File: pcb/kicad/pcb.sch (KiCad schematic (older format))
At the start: 98 parts, among them K00 KEYSW, K01 KEYSW, K02 KEYSW, K03 KEYSW, K04 KEYSW, K05 KEYSW, K10 KEYSW, K11 KEYSW, K12 KEYSW, K13 KEYSW, K14 KEYSW, K15 KEYSW, K20 KEYSW, K21 KEYSW, K22 KEYSW, K23 KEYSW, K24 KEYSW, K25 KEYSW, K33 KEYSW, K34 KEYSW, K35 KEYSW, K40 KEYSW, K41 KEYSW, K42 KEYSW, K43 KEYSW, K44 KEYSW, K45 KEYSW, K50 KEYSW, K51 KEYSW, K52 KEYSW, K53 KEYSW, K54 KEYSW, K55 KEYSW, K60 KEYSW, K61 KEYSW, K62 KEYSW, K63 KEYSW, K64 KEYSW, K65 KEYSW, K70 KEYSW, K71 KEYSW, K72 KEYSW

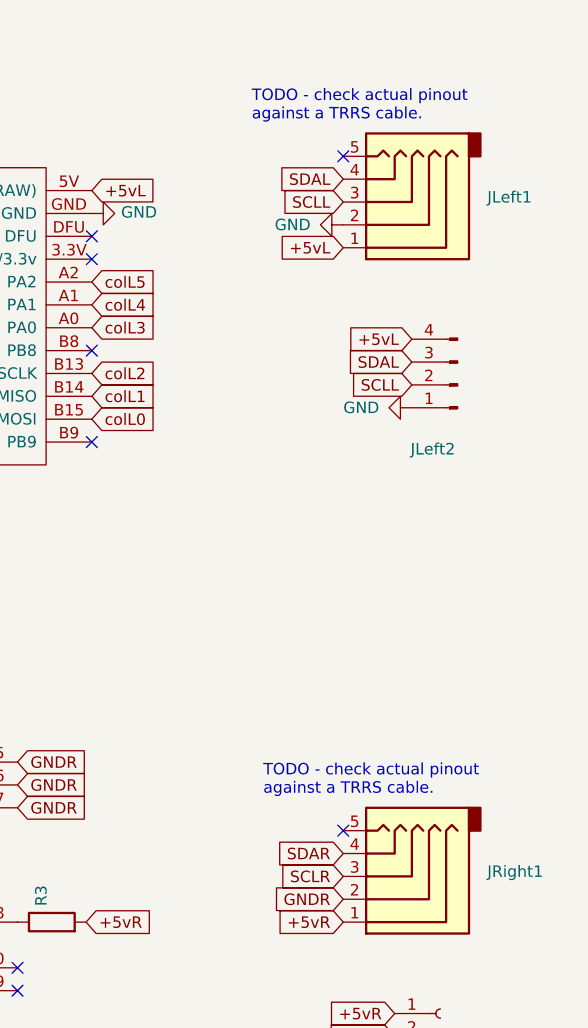
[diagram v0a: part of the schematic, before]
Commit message: PCB: fix wiring of TRRS connectors
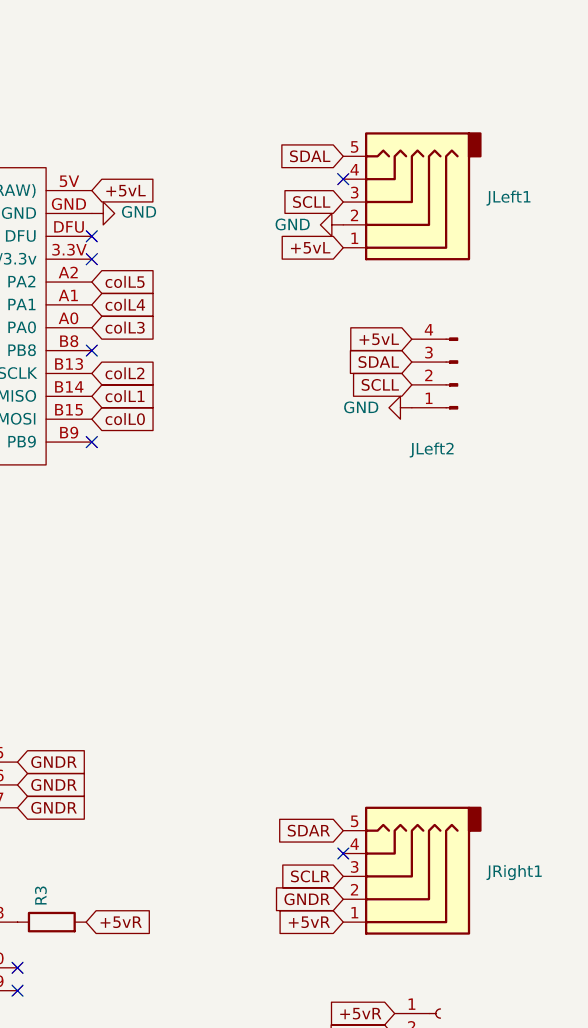
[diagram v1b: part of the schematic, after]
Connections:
- net SDAL: now also JLeft1.5; no longer JLeft1.4
- net SDAR: now also JRight1.5; no longer JRight1.4
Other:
- note removed: "TODO - check actual pinout \nagainst a TRRS cable.\n"
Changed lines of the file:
@@
 	-1   0    0    1
 $EndComp
-Text Notes 10050 1100 0    50   ~ 0
-TODO - check actual pinout \nagainst a TRRS cable.\n
-Text GLabel 10450 1350 0    50   Input ~ 0
-SDAL
 Text GLabel 10450 1450 0    50   Input ~ 0
 SCLL
 Text GLabel 10450 1650 0    50   Input ~ 0
 +5vL
-Text Notes 10100 4050 0    50   ~ 0
-TODO - check actual pinout \nagainst a TRRS cable.\n
 Wire Wire Line
 	8325 5800 8325 6175
@@
 Text GLabel 10450 4400 0    50   Input ~ 0
 SCLR
-Text GLabel 10450 4300 0    50   Input ~ 0
+Text GLabel 10450 4200 0    50   Input ~ 0
 SDAR
 Text GLabel 10450 4600 0    50   Input ~ 0
@@
 NoConn ~ 9350 1700
 NoConn ~ 9350 1600
-NoConn ~ 10450 4200
-NoConn ~ 10450 1250
+NoConn ~ 10450 4300
 NoConn ~ 9350 2500
 $Comp
@@
 	0    1    1    0
 $EndComp
+NoConn ~ 10450 1350
+Text GLabel 10450 1250 0    50   Input ~ 0
+SDAL
 $EndSCHEMATC

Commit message: PCB: increase size of resistor footprints
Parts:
- removed GND (x5): GND, symbol power:GND
- R1, R2, R3: footprint Resistor_THT:R_Axial_DIN0204_L3.6mm_D1.6mm_P5.08mm_Horizontal -> Resistor_THT:R_Axial_DIN0207_L6.3mm_D2.5mm_P7.62mm_Horizontal
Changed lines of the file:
@@
 F 0 "R2" H 9170 6071 50  0000 L CNN
 F 1 "R" H 9170 5980 50  0001 L CNN
-F 2 "Resistor_THT:R_Axial_DIN0204_L3.6mm_D1.6mm_P5.08mm_Horizontal" V 9030 6025 50  0001 C CNN
+F 2 "Resistor_THT:R_Axial_DIN0207_L6.3mm_D2.5mm_P7.62mm_Horizontal" V 9030 6025 50  0001 C CNN
 F 3 "~" H 9100 6025 50  0001 C CNN
 	1    9100 6025
@@
 F 0 "R1" H 9370 5771 50  0000 L CNN
 F 1 "R" H 9370 5680 50  0001 L CNN
-F 2 "Resistor_THT:R_Axial_DIN0204_L3.6mm_D1.6mm_P5.08mm_Horizontal" V 9230 5725 50  0001 C CNN
+F 2 "Resistor_THT:R_Axial_DIN0207_L6.3mm_D2.5mm_P7.62mm_Horizontal" V 9230 5725 50  0001 C CNN
 F 3 "~" H 9300 5725 50  0001 C CNN
 	1    9300 5725
@@
 F 0 "R3" H 9245 4646 50  0000 L CNN
 F 1 "R" H 9245 4555 50  0001 L CNN
-F 2 "Resistor_THT:R_Axial_DIN0204_L3.6mm_D1.6mm_P5.08mm_Horizontal" V 9105 4600 50  0001 C CNN
+F 2 "Resistor_THT:R_Axial_DIN0207_L6.3mm_D2.5mm_P7.62mm_Horizontal" V 9105 4600 50  0001 C CNN
 F 3 "~" H 9175 4600 50  0001 C CNN
 	1    9175 4600
@@
 NoConn ~ 9350 2500
 $Comp
-L power:GND GND
+L power:GND #GND0101
 U 1 1 5E7A8207
 P 9350 1500
-F 0 "GND" H 9350 1250 50  0001 C CNN
+F 0 "#GND0101" H 9350 1250 50  0001 C CNN
 F 1 "GND" V 9355 1372 50  0000 R CNN
 F 2 "" H 9350 1500 50  0001 C CNN
@@
 $EndComp
 $Comp
-L power:GND GND
+L power:GND #GND0102
 U 1 1 5E7B0C54
 P 10450 1550
-F 0 "GND" H 10450 1300 50  0001 C CNN
+F 0 "#GND0102" H 10450 1300 50  0001 C CNN
 F 1 "GND" V 10450 1250 50  0000 L CNN
 F 2 "" H 10450 1550 50  0001 C CNN
@@
 $EndComp
 $Comp
-L power:GND GND
+L power:GND #GND0103
 U 1 1 5E7B852F
 P 7300 1600
-F 0 "GND" H 7300 1350 50  0001 C CNN
+F 0 "#GND0103" H 7300 1350 50  0001 C CNN
 F 1 "GND" V 7300 1300 50  0000 L CNN
 F 2 "" H 7300 1600 50  0001 C CNN
@@
 $EndComp
 $Comp
-L power:GND GND
+L power:GND #GND0104
 U 1 1 5E7BB358
 P 7300 1700
-F 0 "GND" H 7300 1450 50  0001 C CNN
+F 0 "#GND0104" H 7300 1450 50  0001 C CNN
 F 1 "GND" V 7300 1400 50  0000 L CNN
 F 2 "" H 7300 1700 50  0001 C CNN
@@
 $EndComp
 $Comp
-L power:GND GND
+L power:GND #GND0105
 U 1 1 5E7C1CBE
 P 10750 2350
-F 0 "GND" H 10750 2100 50  0001 C CNN
+F 0 "#GND0105" H 10750 2100 50  0001 C CNN
 F 1 "GND" V 10750 2050 50  0000 L CNN
 F 2 "" H 10750 2350 50  0001 C CNN

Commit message: PCB: Fix position of female pin connector
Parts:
- JLeft2: footprint 42_keyboard:Conn-1x4 -> 42_keyboard:Conn-1x4-Male
- JRight2: footprint 42_keyboard:Conn-1x4 -> 42_keyboard:Conn-1x4-Female
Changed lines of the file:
@@
 F 0 "JLeft2" H 11058 2531 50  0000 C CNN
 F 1 "Conn_01x04_Male" H 11058 2440 50  0001 C CNN
-F 2 "42_keyboard:Conn-1x4" H 10950 2250 50  0001 C CNN
+F 2 "42_keyboard:Conn-1x4-Male" H 10950 2250 50  0001 C CNN
 F 3 "~" H 10950 2250 50  0001 C CNN
 	1    10950 2250
@@
 F 0 "JRight2" H 10903 5076 50  0000 L CNN
 F 1 "Conn_01x04_Female" H 10903 4985 50  0001 L CNN
-F 2 "42_keyboard:Conn-1x4" H 10875 5100 50  0001 C CNN
+F 2 "42_keyboard:Conn-1x4-Female" H 10875 5100 50  0001 C CNN
 F 3 "~" H 10875 5100 50  0001 C CNN
 	1    10875 5100
